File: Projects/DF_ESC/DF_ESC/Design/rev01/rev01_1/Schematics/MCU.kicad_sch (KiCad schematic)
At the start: 0 parts

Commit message: Update 05
Added the stm32 microcontroller to the schematics with its decoupling caps
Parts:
- added C1: 100n, symbol Device:C
- added C2, C3, C4, C5, C6: C, symbol Device:C
- added C7: 10u, symbol Device:C
- added U1: STM32F405RGTx, Package_QFP:LQFP-64_10x10mm_P0.5mm, symbol MCU_ST_STM32F4:STM32F405RGTx
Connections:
- new net: U1.18 (VSS), U1.63 (VSS)
- new net +3V3: C1.1, C2.1, C3.1, C4.1, C5.1, C6.1, C7.1, U1.13 (VDDA), U1.19 (VDD), U1.32 (VDD), U1.48 (VDD), U1.64 (VDD)
- new net GND: C1.2, C2.2, C3.2, C4.2, C5.2, C6.2, C7.2
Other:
- note added: "${TITLE}"
- title: (none) -> [04] - MCU

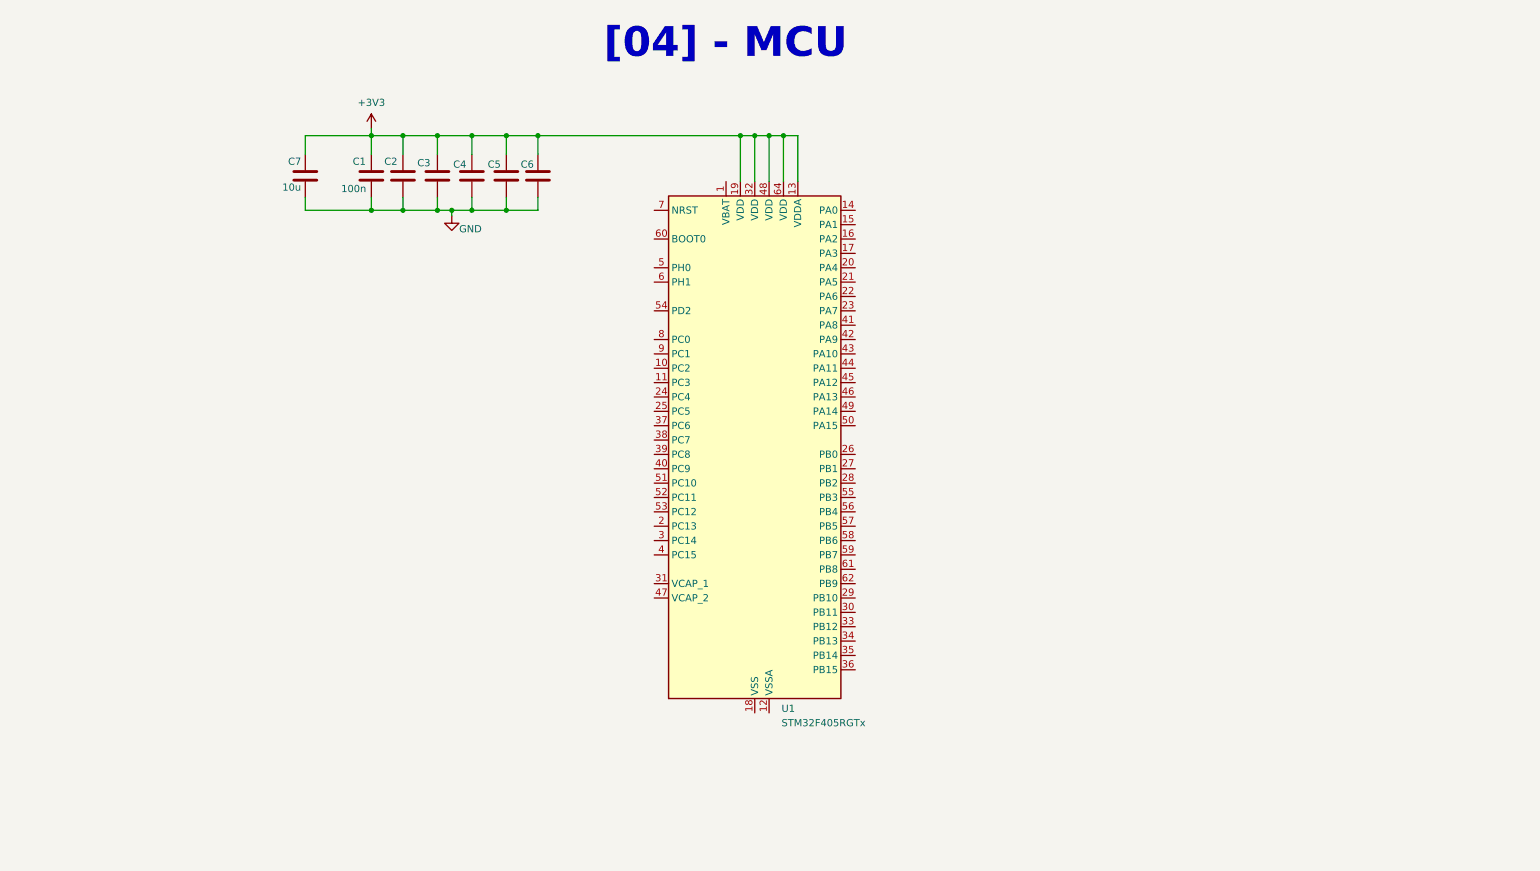
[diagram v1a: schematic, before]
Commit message: Update 06
Completed the MCU schematics
temp
input voltage scaling
comms
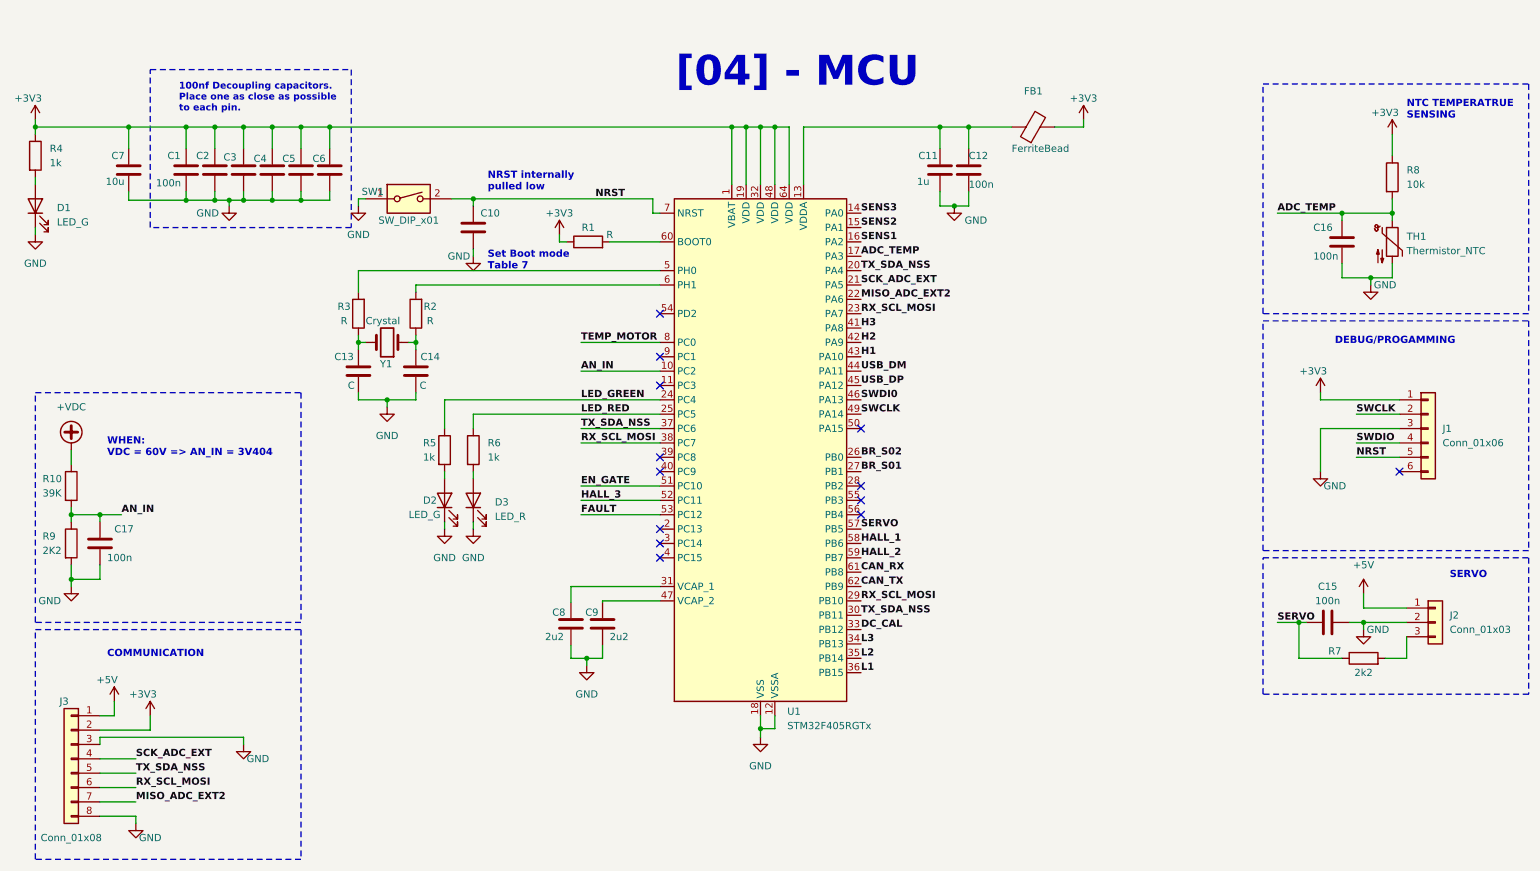
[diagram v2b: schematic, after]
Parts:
- added C10, C13, C14: C, symbol Device:C
- added C11: 1u, symbol Device:C
- added C12, C15, C16, C17: 100n, symbol Device:C
- added C8, C9: 2u2, symbol Device:C
- added D1, D2: LED_G, symbol Device:LED
- added D3: LED_R, symbol Device:LED
- added FB1: FerriteBead, symbol Device:FerriteBead
- added J1: Conn_01x06, symbol Connector_Generic:Conn_01x06
- added J2: Conn_01x03, symbol Connector_Generic:Conn_01x03
- added J3: Conn_01x08, symbol Connector_Generic:Conn_01x08
- added R1, R2, R3: R, symbol Device:R
- added R10: 39K, symbol Device:R
- added R4, R5, R6: 1k, symbol Device:R
- added R7: 2k2, symbol Device:R
- added R8: 10k, symbol Device:R
- added R9: 2K2, symbol Device:R
- added SW1: SW_DIP_x01, symbol Switch:SW_DIP_x01
- added TH1: Thermistor_NTC, symbol Device:Thermistor_NTC
- added Y1: Crystal, symbol Device:Crystal
- C2, C3, C4, C5, C6: value C -> 100n
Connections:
- net +3V3: now also U1.1 (VBAT), FB1.2, J1.1 (Pin_1), J3.2 (Pin_2), R1.1, R4.1, R8.1; no longer U1.13 (VDDA)
- net GND: now also U1.12 (VSSA), U1.18 (VSS), U1.63 (VSS), C10.2, C11.2, C12.2, C13.1, C14.1, C15.2, C16.2, C17.2, C8.2, C9.2, D1.1 (K), D2.1 (K), D3.1 (K), J1.3 (Pin_3), J2.2 (Pin_2), J3.3 (Pin_3), J3.8 (Pin_8), R9.2, SW1.1, TH1.2
- net AN_IN: now reaches U1.10 (PC2)
- net AN_IN: now also C17.1, R10.2, R9.1
- net SENS3: now reaches U1.14 (PA0)
- net SENS2: now reaches U1.15 (PA1)
- net SENS1: now reaches U1.16 (PA2)
- net ADC_TEMP: now reaches U1.17 (PA3)
- net ADC_TEMP: now also C16.1, R8.2, TH1.1
- net TX_SDA_NSS: now reaches U1.20 (PA4)
- net TX_SDA_NSS: now also U1.30 (PB11), U1.37 (PC6), J3.5 (Pin_5)
- net SCK_ADC_EXT: now reaches U1.21 (PA5)
- net SCK_ADC_EXT: now also J3.4 (Pin_4)
- net MISO_ADC_EXT2: now reaches U1.22 (PA6)
- net MISO_ADC_EXT2: now also J3.7 (Pin_7)
- net RX_SCL_MOSI: now reaches U1.23 (PA7)
- net RX_SCL_MOSI: now also U1.29 (PB10), U1.38 (PC7), J3.6 (Pin_6)
- net LED_GREEN: now reaches U1.24 (PC4)
- net LED_GREEN: now also R5.1
- net LED_RED: now reaches U1.25 (PC5)
- net LED_RED: now also R6.1
- net BR_S02: now reaches U1.26 (PB0)
- net BR_S01: now reaches U1.27 (PB1)
- net at U1.31 (VCAP_1): now also C8.1
- net DC_CAL: now reaches U1.33 (PB12)
- net L3: now reaches U1.34 (PB13)
- net L2: now reaches U1.35 (PB14)
- net L1: now reaches U1.36 (PB15)
- net H3: now reaches U1.41 (PA8)
- net H2: now reaches U1.42 (PA9)
- net H1: now reaches U1.43 (PA10)
- net USB_DM: now reaches U1.44 (PA11)
- net USB_DP: now reaches U1.45 (PA12)
- net SWDI0: now reaches U1.46 (PA13)
- net at U1.47 (VCAP_2): now also C9.1
- net SWCLK: now reaches U1.49 (PA14)
- net SWCLK: now also J1.2 (Pin_2)
- net at U1.5 (PH0): now also R3.2
- net EN_GATE: now reaches U1.51 (PC10)
- net HALL_3: now reaches U1.52 (PC11)
- net FAULT: now reaches U1.53 (PC12)
- net SERVO: now reaches U1.57 (PB5)
- net SERVO: now also C15.1, R7.1
- net HALL_1: now reaches U1.58 (PB6)
- net HALL_2: now reaches U1.59 (PB7)
- net at U1.6 (PH1): now also R2.2
- net at U1.60 (BOOT0): now also R1.2
- net CAN_RX: now reaches U1.61 (PB8)
- net CAN_TX: now reaches U1.62 (PB9)
- net NRST: now reaches U1.7 (NRST)
- net NRST: now also C10.1, J1.5 (Pin_5), SW1.2
- net TEMP_MOTOR: now reaches U1.8 (PC0)
- new net: D3.2 (A), R6.2
- new net: C11.1, C12.1, FB1.1, U1.13 (VDDA)
- new net: J2.3 (Pin_3), R7.2
- new net: C14.2, R2.1, Y1.1
- new net: D1.2 (A), R4.2
- new net: C13.2, R3.1, Y1.2
- new net: D2.2 (A), R5.2
- new net +5V: J2.1 (Pin_1), J3.1 (Pin_1)
- new net +VDC: R10.1
- new net SWDIO: J1.4 (Pin_4)
- no-connect marks 0 -> 13
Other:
- note added: "100nf Decoupling capacitors. Place one as close as possible to each pin."
- note added: "COMMUNICATION"
- note added: "DEBUG/PROGAMMING"
- note added: "NRST internally pulled low"
- note added: "NTC TEMPERATRUE SENSING"
- note added: "SERVO"
- note added: "Set Boot mode Table 7"
- note added: "WHEN: VDC = 60V => AN_IN = 3V404"
- moved on the sheet: C1, C2, C3, C4, C5, C6, C7, U1
